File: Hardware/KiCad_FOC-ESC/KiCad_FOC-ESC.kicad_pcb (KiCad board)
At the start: 4 copper layers, 41 x 41 mm, 46 parts, among them IC1 DRV8300DPWR, IC2 TSC1801BILT, IC3 TSC1801BILT, IC4 TSC1801BILT, IC5 REF2030AIDDCR, IC6 MA702GQ-P, Q1 NTTFS5D6N08XLTAG, Q2 NTTFS5D6N08XLTAG, Q3 NTTFS5D6N08XLTAG, Q4 NTTFS5D6N08XLTAG, Q5 NTTFS5D6N08XLTAG, Q6 NTTFS5D6N08XLTAG, U1 STM32G473RCTx, U3 MT6701CT, U802 ZLDO1117Q, Y1 ASDDV-16.000MHZ-LR-T

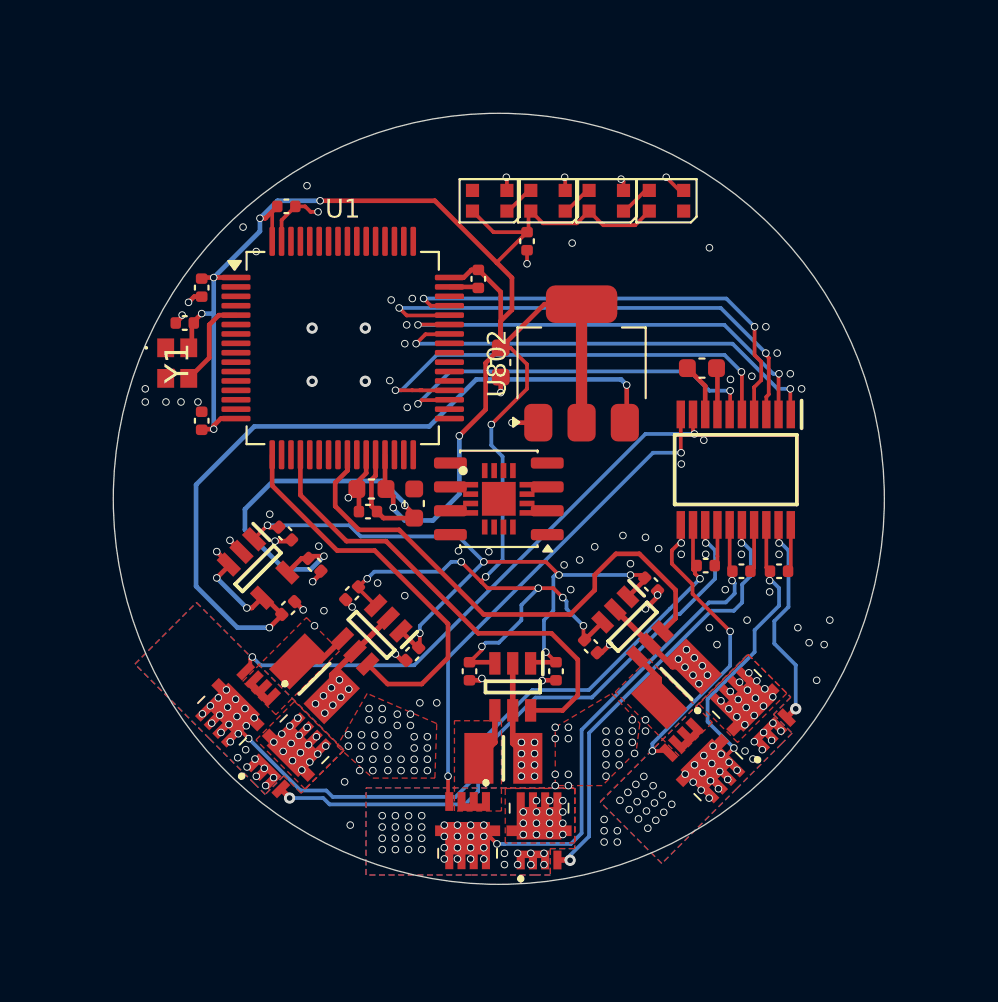
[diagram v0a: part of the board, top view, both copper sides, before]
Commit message: changed formfactor, driver, output stage (#14)
Co-authored-by: CTTOSP <255604560+CTTOSP@users.noreply.github.com>
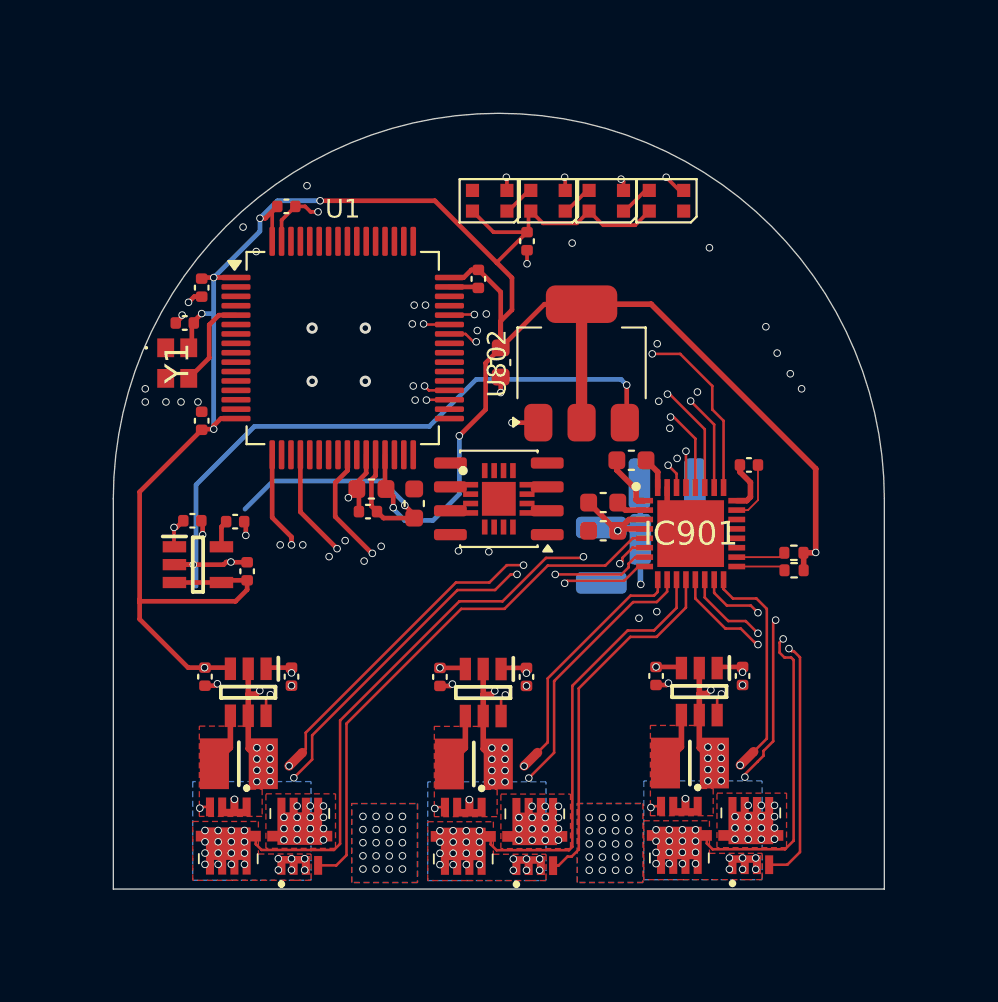
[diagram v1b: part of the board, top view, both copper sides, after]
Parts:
- removed C18: 1uF, Capacitor_SMD:C_0603_1608Metric
- removed C21, C22, C23: 100nF, Capacitor_SMD:C_0402_1005Metric
- removed IC1: DRV8300DPWR, SamacSys_Parts:SOP65P640X120-20N
- added C110: 4.7u, SamacSys_Parts:C_1210_3225Metric_DC_LINK, B.Cu at (153.5, 98.4)
- added C116: 4.7u, SamacSys_Parts:C_1210_3225Metric_DC_LINK, B.Cu at (153.4, 95.5)
- added C122: 4.7u, SamacSys_Parts:C_1210_3225Metric_DC_LINK, B.Cu at (149.9, 99.2)
- added C901: 1uF, Capacitor_SMD:C_0402_1005Metric, F.Cu at (157.8, 94.5)
- added C902: 1uF, Capacitor_SMD:C_0603_1608Metric, F.Cu at (150.1, 96.5)
- added C903: 100nF, Capacitor_SMD:C_0603_1608Metric, F.Cu at (150.1, 98.0)
- added C904: 47nF, Capacitor_SMD:C_0603_1608Metric, F.Cu at (151.6, 94.2)
- added IC901: DRV8320SRTVR, SamacSys_Parts:QFN50P500X500X80-33N-D, F.Cu at (154.7, 98.1)
- added NT1: NetTie_2, NetTie:NetTie-2_SMD_Pad0.5mm, F.Cu at (133.7, 110.1)
- added NT2: NetTie_2, NetTie:NetTie-2_SMD_Pad0.5mm, F.Cu at (146.2, 110.1)
- added NT3: NetTie_2, NetTie:NetTie-2_SMD_Pad0.5mm, F.Cu at (157.7, 110.0)
- added R901: 10kR, Resistor_SMD:R_0402_1005Metric, F.Cu at (160.2, 99.1)
- added R902: 10kR, Resistor_SMD:R_0402_1005Metric, F.Cu at (160.2, 100.0)
- moved Q2 25.5 mm to (130.1, 114.1), turned to 180 degrees
- moved Q1 25.1 mm to (133.9, 114.2), turned to 0 degrees
- moved Q5 25.0 mm to (157.9, 114.2), turned to 0 degrees
- moved Q6 24.4 mm to (154.1, 114.1), turned to 180 degrees
- moved R4 23.7 mm to (130.7, 110.3), turned to 180 degrees
- moved IC2 20.7 mm to (131.2, 106.5), turned to -90 degrees
- moved C10 20.6 mm to (128.9, 105.7), turned to -90 degrees
- moved R6 20.5 mm to (154.7, 110.3), turned to 180 degrees
- moved C14 19.7 mm to (133.5, 105.7), turned to -90 degrees
- moved IC4 17.7 mm to (155.2, 106.5), turned to -90 degrees
- moved C16 17.6 mm to (157.5, 105.7), turned to -90 degrees
- moved C12 16.8 mm to (152.9, 105.7), turned to -90 degrees
- moved C17 4.98 mm to (128.2, 97.4), turned to 180 degrees
- moved C19 4.80 mm to (130.5, 97.5), turned to 180 degrees
- moved IC5 3.21 mm to (128.5, 99.8), turned to 0 degrees
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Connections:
- net /FETs/HalfBridgeA/GND1 renamed SLA
- net /FETs/HalfBridgeB/GND1 renamed SLB
- net /FETs/HalfBridgeC/GND1 renamed SLC
- C13 pad 2: +5V -> +3V3
- IC5 pad 3: +5V -> +3V3
- IC5 pad 4: +5V -> +3V3
- U1 pad 17: OUT3 -> OUT1
- U1 pad 25: OUT1 -> OUT3
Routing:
- net +3V3: track 129.0 -> 171.4 mm, vias 15 -> 11
- net VCC: track 0.00 -> 35.6 mm, vias 79 -> 67
- net /FETs/DRV8320S_1/SPA: track 0.00 -> 24.0 mm, vias 0 -> 2
- net GHA: track 11.5 -> 28.7 mm, vias 2 -> 0
- net SHA: track 16.3 -> 32.1 mm, vias 42 -> 24
- net GLA: track 16.2 -> 30.7 mm, vias 3 -> 4
- net OUT1: track 28.6 -> 14.9 mm, vias 0 -> 2
- net SHC: track 35.9 -> 22.7 mm, vias 26 -> 24
- net /FETs/DRV8320S_1/SPB: track 0.00 -> 12.6 mm
- net GHC: track 32.7 -> 20.2 mm
- net +5V: track 45.2 -> 32.8 mm, vias 5 -> 1
- net /FETs/DRV8320S_1/SPC: track 0.00 -> 11.1 mm
- net GLC: track 30.7 -> 20.0 mm, vias 2 -> 4
- net OUT3: track 21.1 -> 29.5 mm, vias 0 -> 2
- net +3V: track 24.7 -> 17.4 mm, vias 2 -> 1
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- added copper zone on In3.Cu, net GND
- added copper zone on In4.Cu, net GND
- added copper zone on B.Cu, net VCC
- added copper zone on In1.Cu, net VCC
- added copper zone on In3.Cu, net VCC
- added copper zone on In4.Cu, net VCC
- removed copper zone on In1.Cu, net SHA
- removed copper zone on In2.Cu, net SHA
- removed copper zone on In1.Cu, net SHB
- removed copper zone on In2.Cu, net SHB
- removed copper zone on In1.Cu, net SHC
- removed copper zone on In2.Cu, net SHC
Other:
- board size 41 x 41 mm -> 41 x 41.2 mm
- copper layers 4 -> 6

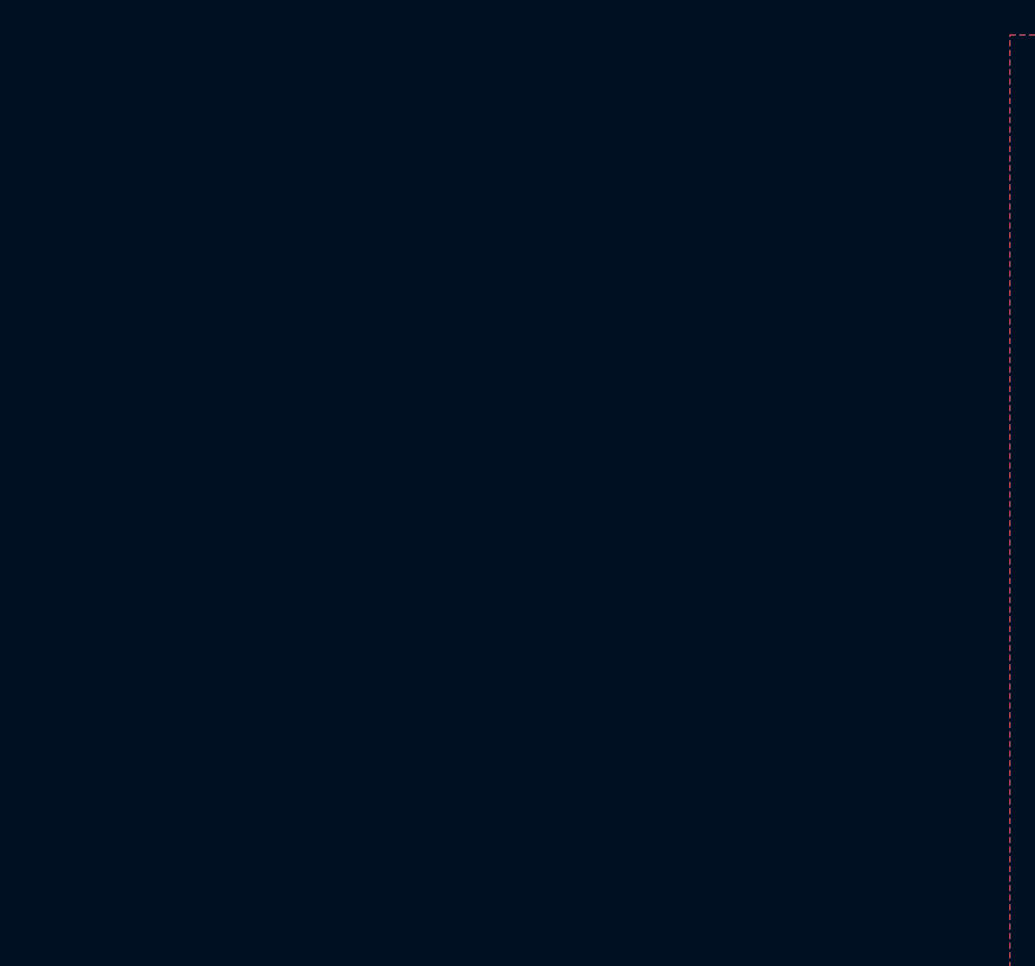
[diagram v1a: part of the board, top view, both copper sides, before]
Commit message: stator prototype 1 finished
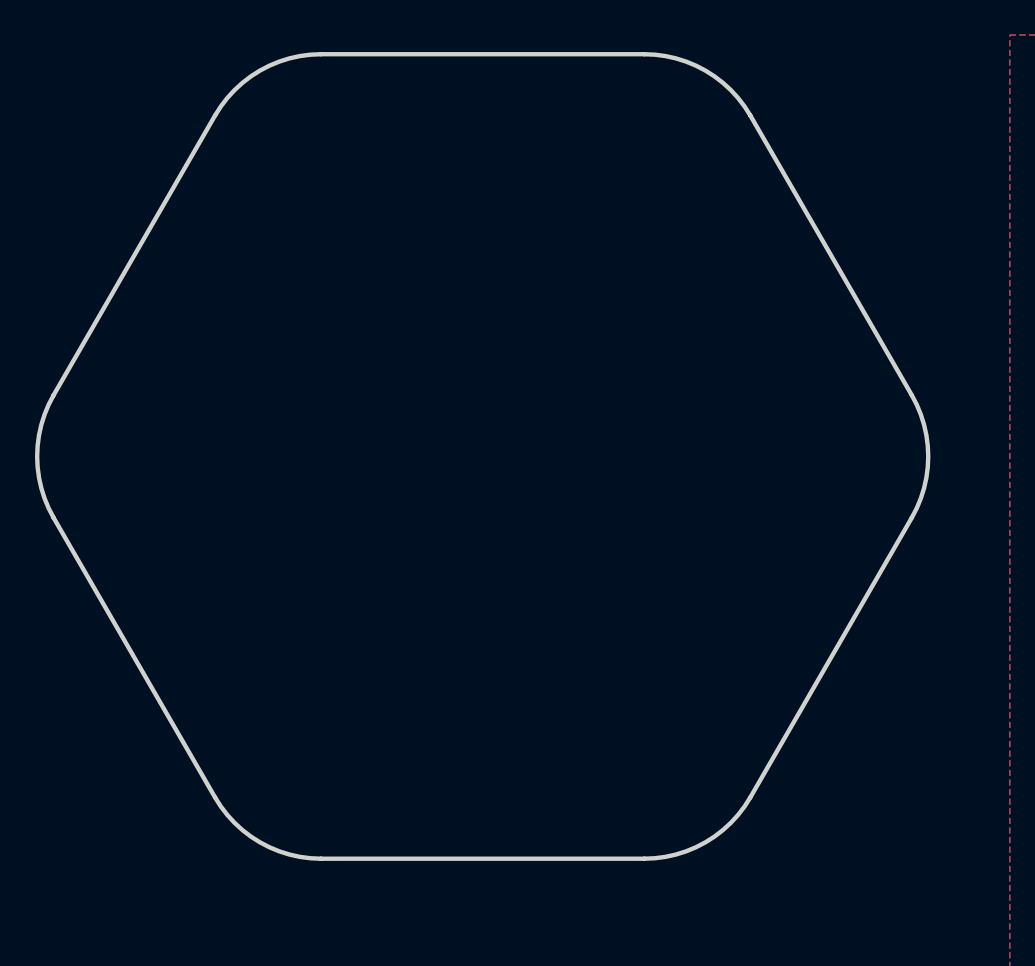
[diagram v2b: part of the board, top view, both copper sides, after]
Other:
- board size 41 x 41.2 mm -> 140.6 x 65.9 mm

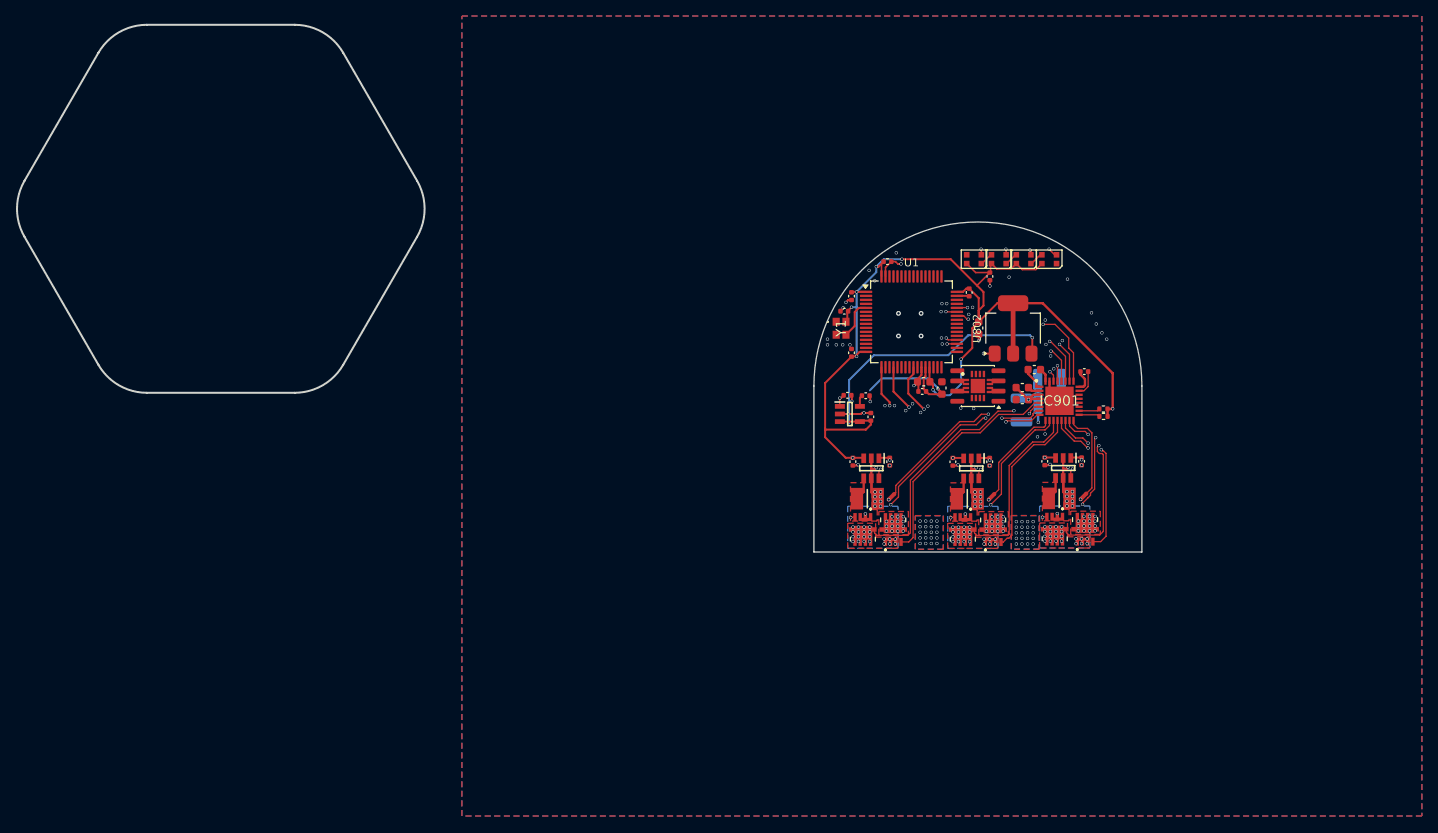
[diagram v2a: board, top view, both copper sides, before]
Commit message: edited formfactor (#16)
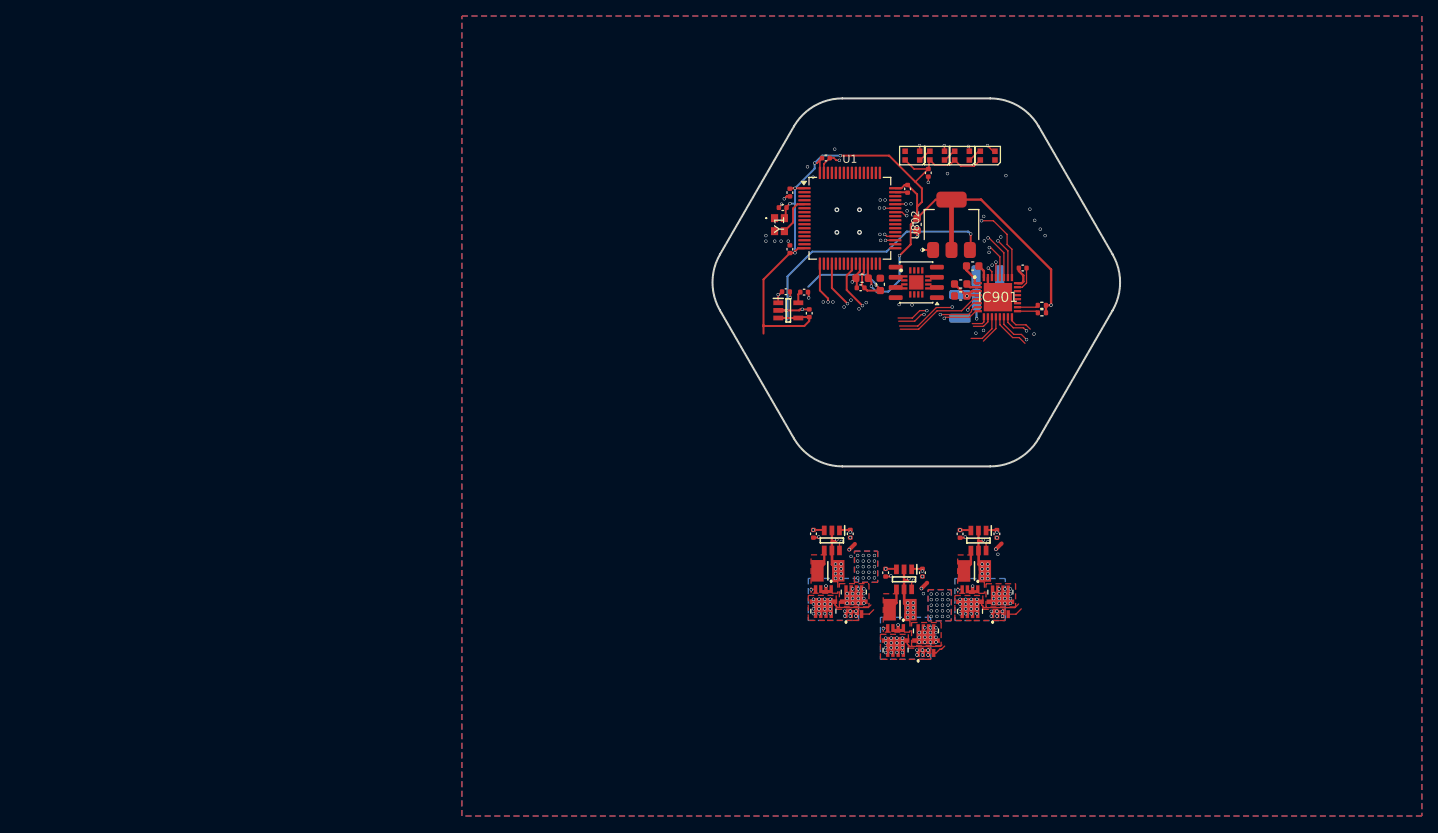
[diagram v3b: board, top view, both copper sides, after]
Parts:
- moved Q4 16.2 mm to (134.2, 128.0)
- moved C11 16.2 mm to (133.0, 119.6)
- moved C15 16.2 mm to (137.6, 119.6)
- moved IC3 16.2 mm to (135.3, 120.4)
- moved Q3 16.2 mm to (138.0, 128.1)
- moved R5 16.2 mm to (134.8, 124.2)
- moved C110 15.1 mm to (145.8, 85.5)
- moved C7 15.1 mm to (138.3, 69.6)
- moved C9 15.1 mm to (129.8, 84.0)
- moved C901 15.1 mm to (150.1, 81.5)
- moved C902 15.1 mm to (142.3, 83.5)
- moved C903 15.1 mm to (142.3, 85.0)
- moved C904 15.1 mm to (143.8, 81.2)
- moved D3 15.1 mm to (142.5, 67.5)
- moved U802 15.1 mm to (141.2, 76.1)
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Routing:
- net +3V3: track 171.4 -> 137.6 mm
- net +1V5: track 43.1 -> 15.5 mm
- net GHA: track 28.7 -> 13.0 mm
- net SHA: track 32.1 -> 16.6 mm
- net OUT3: track 29.5 -> 15.6 mm
- net GHB: track 19.2 -> 5.41 mm
- net GHC: track 20.2 -> 7.01 mm, vias 2 -> 0
- net SHC: track 22.7 -> 9.92 mm, vias 24 -> 23
- net SHB: track 22.3 -> 9.57 mm
- net /FETs/DRV8320S_1/SPA: track 24.0 -> 11.6 mm
- net GLA: track 30.7 -> 19.8 mm
- net VCC: track 35.6 -> 24.9 mm, vias 67 -> 47
- net /FETs/DRV8320S_1/SPB: track 12.6 -> 2.18 mm
- net GLB: track 20.7 -> 11.8 mm
- net /FETs/DRV8320S_1/SPC: track 11.1 -> 3.23 mm
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- removed copper zone on B.Cu, net VCC
- removed copper zone on In1.Cu, net VCC
- removed copper zone on In3.Cu, net VCC
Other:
- board size 140.6 x 65.9 mm -> 51 x 46 mm
